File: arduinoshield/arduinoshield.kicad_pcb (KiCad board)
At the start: 2 copper layers, 68.6 x 53.3 mm, 21 parts, among them J1 Gas_sensor_AIME, J2 LTC1050, P1 Power, P2 Analog, P3 Digital, P4 Digital, P5 CONN_01X01, P6 CONN_01X01, P7 CONN_01X01, P8 CONN_01X01

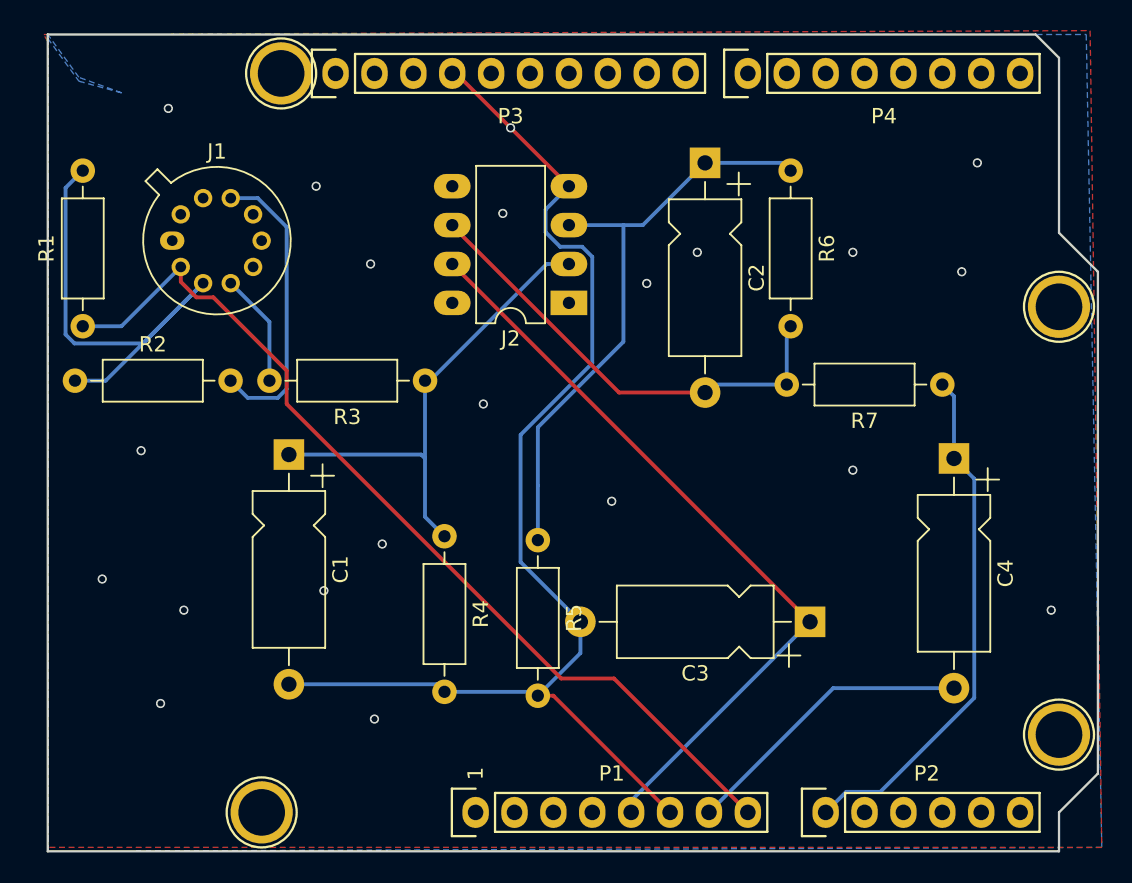
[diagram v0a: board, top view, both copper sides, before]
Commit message: add lora headers
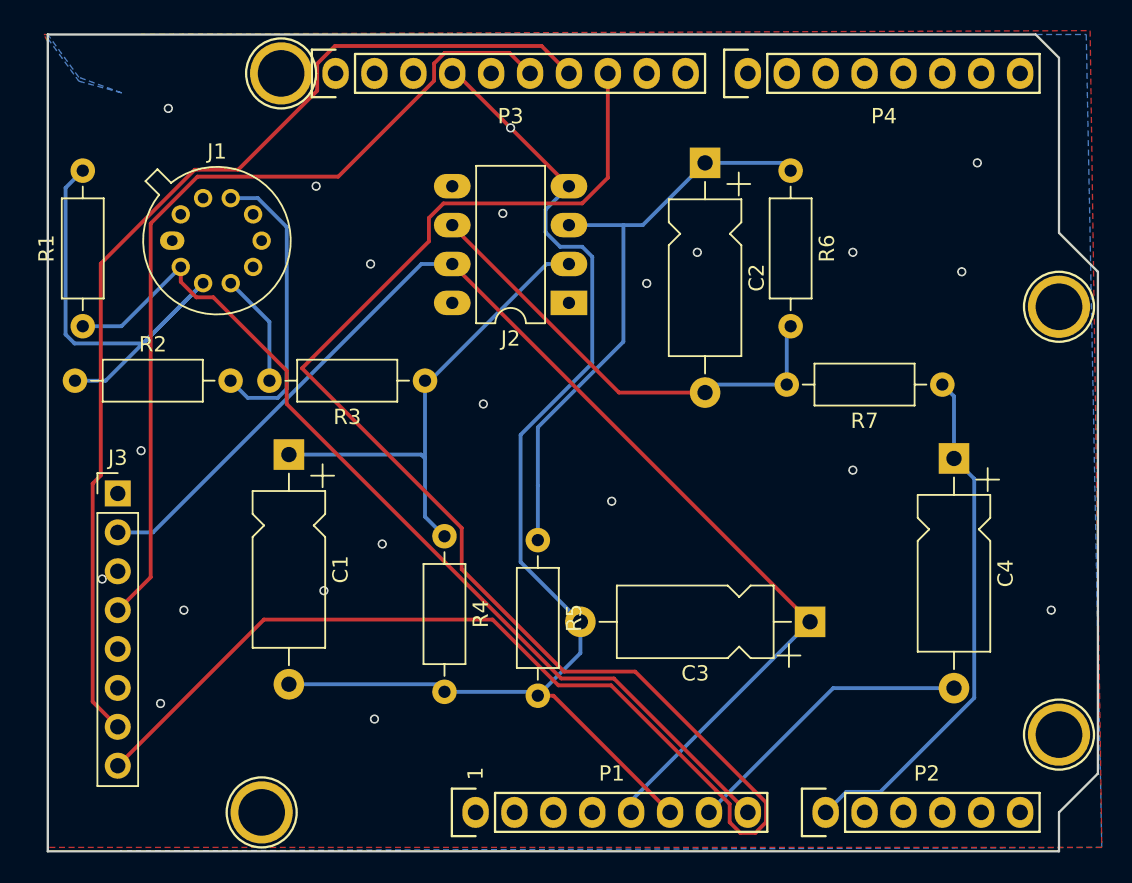
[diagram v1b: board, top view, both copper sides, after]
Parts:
- added J3: Conn_01x08_Female, Connector_PinHeader_2.54mm:PinHeader_1x08_P2.54mm_Vertical, F.Cu at (115.6, 103.0)
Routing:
- net /10(**/SS): track 0.00 -> 130.8 mm
- net /11(**/MOSI): track 0.00 -> 69.4 mm
- net /12(MISO): track 0.00 -> 56.7 mm
- net +5V: track 50.3 -> 79.4 mm
- net GND: vias 20 -> 21
- net (no net): vias 1 -> 0
